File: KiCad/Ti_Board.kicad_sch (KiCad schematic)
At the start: 0 parts

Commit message: 24OCT23
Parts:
- added J8: CAN Connector, symbol Connector_Generic:Conn_02x06_Counter_Clockwise
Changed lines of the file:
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@@
 (kicad_sch (version 20230121) (generator eeschema)
   (paper "A4")
+  (symbol (lib_id "Connector_Generic:Conn_02x06_Counter_Clockwise") (at 118.11 50.8 0) (mirror y) (unit 1)
+    (in_bom yes) (on_board yes) (dnp no)
+    (property "Reference" "J8" (at 119.3801 55.88 90)
+      (effects (font (size 1.27 1.27)) (justify right))
+    )
+    (property "Value" "CAN Connector" (at 109.22 62.23 0)
+      (effects (font (size 1.27 1.27)) (justify right))
+    )
+    (property "Footprint" "" (at 118.11 50.8 0)
+      (effects (font (size 1.27 1.27)) hide)
+    )
+    (property "Datasheet" "~" (at 118.11 50.8 0)
+      (effects (font (size 1.27 1.27)) hide)
+    )
+    (pin "1")
+    (pin "10")
+    (pin "11")
+    (pin "12")
+    (pin "2")
+    (pin "3")
+    (pin "4")
+    (pin "5")
+    (pin "6")
+    (pin "7")
+    (pin "8")
+    (pin "9")
+    (instances
+      (project "Car_TractiveSystem_v2"
+        (path "/588b5c14-1813-4e1d-9dbe-940839ecebe3"
+          (reference "J8") (unit 1)
+        )
+        (path "/588b5c14-1813-4e1d-9dbe-940839ecebe3/42103732-fa28-467e-b394-54af70cbf903"
+          (reference "J3") (unit 1)
+        )
+      )
+    )
+  )
 )

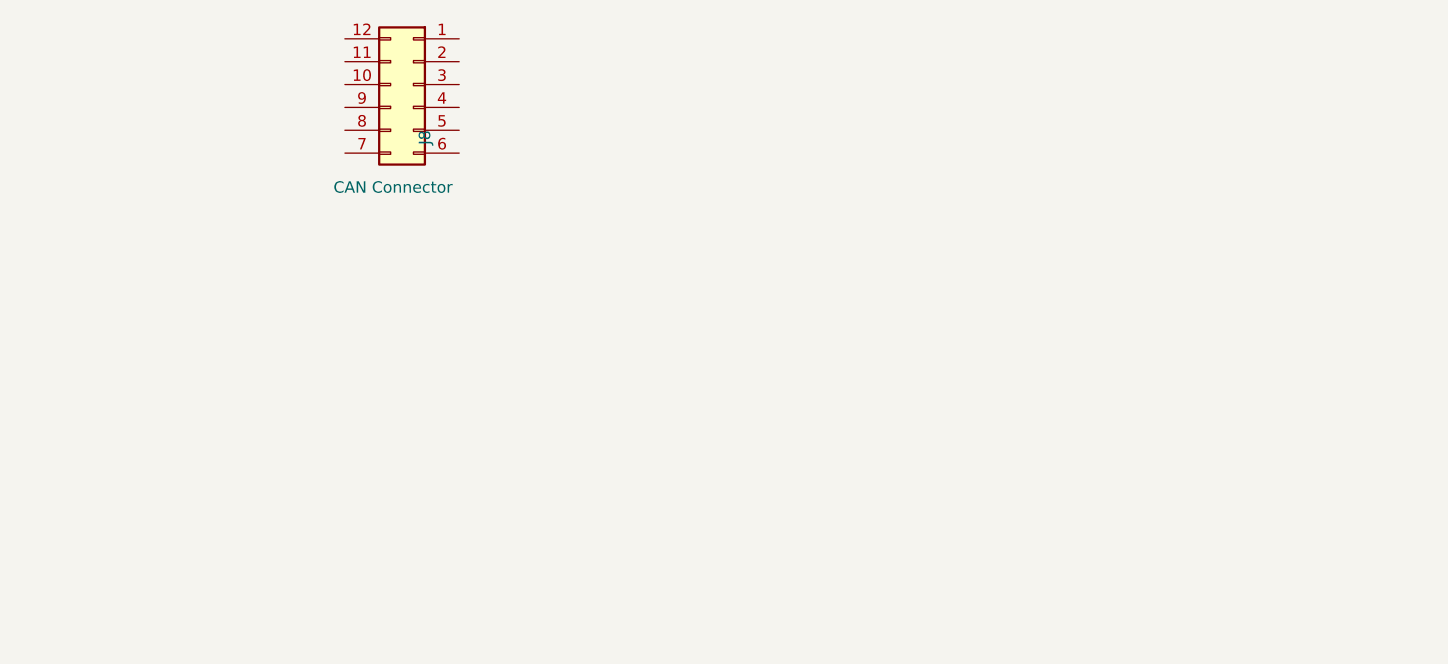
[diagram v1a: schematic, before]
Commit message: Update Ti_Board.kicad_sch
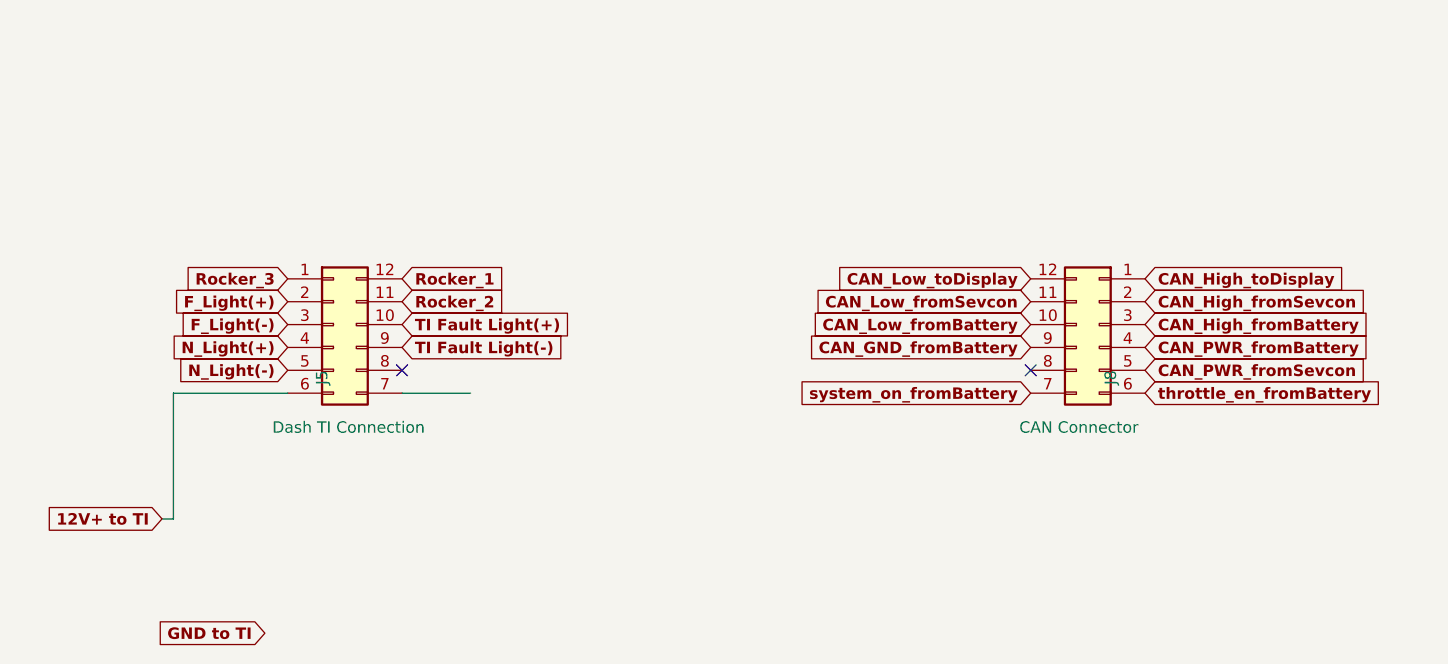
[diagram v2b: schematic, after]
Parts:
- added J5: Dash TI Connection, symbol Connector_Generic:Conn_02x06_Counter_Clockwise
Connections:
- net CAN_High_toDisplay: now reaches J8.1 (Pin_1)
- net CAN_Low_fromBattery: now reaches J8.10 (Pin_10)
- net CAN_Low_fromSevcon: now reaches J8.11 (Pin_11)
- net CAN_Low_toDisplay: now reaches J8.12 (Pin_12)
- net CAN_High_fromSevcon: now reaches J8.2 (Pin_2)
- net CAN_High_fromBattery: now reaches J8.3 (Pin_3)
- net CAN_PWR_fromBattery: now reaches J8.4 (Pin_4)
- net CAN_PWR_fromSevcon: now reaches J8.5 (Pin_5)
- net throttle_en_fromBattery: now reaches J8.6 (Pin_6)
- net system_on_fromBattery: now reaches J8.7 (Pin_7)
- net CAN_GND_fromBattery: now reaches J8.9 (Pin_9)
- new net 12V+ to TI: J5.6 (Pin_6)
- new net F_Light(+): J5.2 (Pin_2)
- new net F_Light(-): J5.3 (Pin_3)
- new net N_Light(+): J5.4 (Pin_4)
- new net N_Light(-): J5.5 (Pin_5)
- new net Rocker_1: J5.12 (Pin_12)
- new net Rocker_2: J5.11 (Pin_11)
- new net Rocker_3: J5.1 (Pin_1)
- new net TI Fault Light(+): J5.10 (Pin_10)
- new net TI Fault Light(-): J5.9 (Pin_9)
- no-connect marks 0 -> 2
